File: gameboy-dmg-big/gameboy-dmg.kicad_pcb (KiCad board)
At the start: 2 copper layers, 82.5 x 139.7 mm, 95 parts, among them J1 Conn_01x02, J2 USB_A, J3 Conn_01x08, J4 Conn_01x04, J5 Raspberry_Pi_2_3, J7 USB_B_Micro, J8 Conn_01x02, P1 RK10J_POT, Q1 S8050, SW1 SW_DPDT_x2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

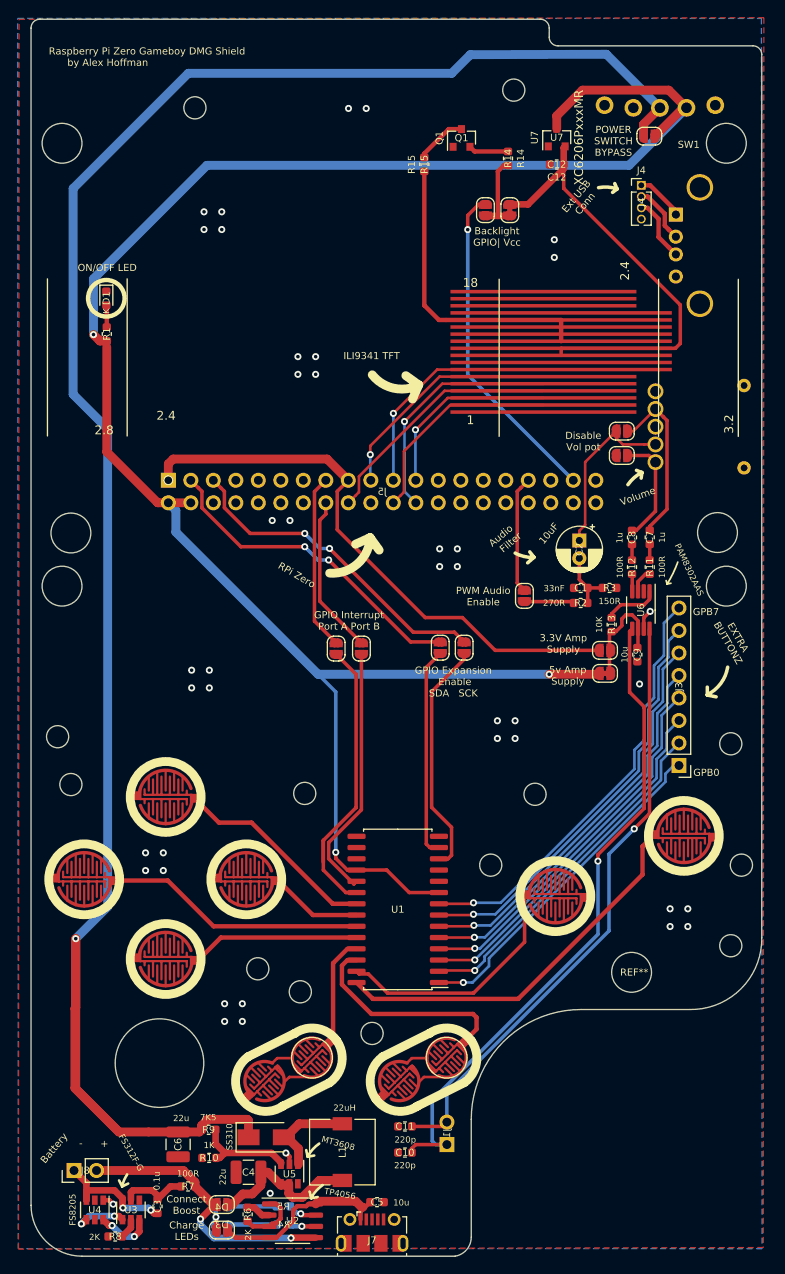
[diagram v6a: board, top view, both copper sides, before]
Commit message: Updated PCBs from initial debugging
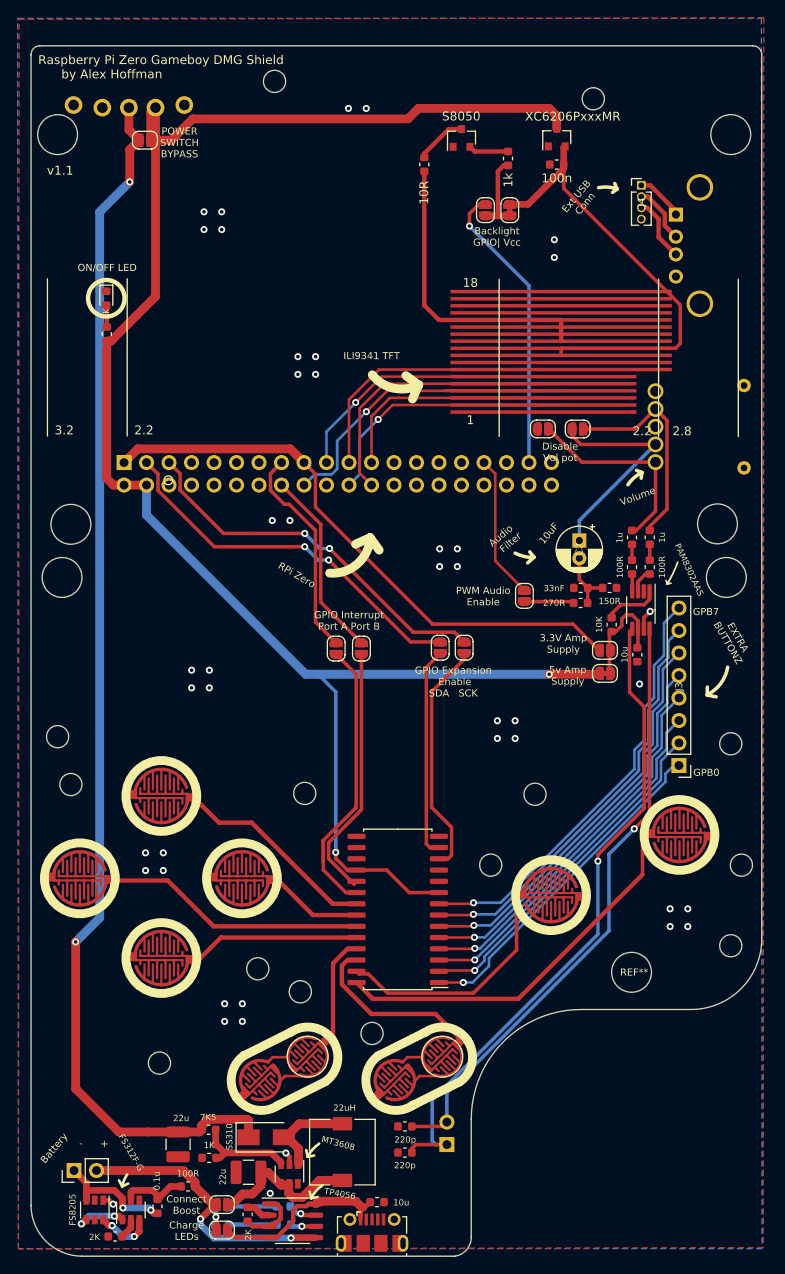
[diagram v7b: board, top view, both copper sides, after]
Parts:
- removed the REF** at (82.5, 77.1)
- removed the REF** at (133.5, 21.1)
- removed the REF** at (97.5, 23.1)
- removed the REF** at (157.5, 27.1)
- removed the REF** at (82.5, 27.1)
- removed the REF** at (83.5, 71.1)
- added REF**: MountingHole_2.5mm, MountingHole:MountingHole_2.5mm, F.Cu at (106.5, 20.1)
- added REF**: MountingHole_4.5mm, MountingHole:MountingHole_4.5mm, F.Cu at (82.5, 76.1)
- added REF**: MountingHole_2.5mm, MountingHole:MountingHole_2.5mm, F.Cu at (142.5, 22.1)
- added REF**: MountingHole_4.5mm, MountingHole:MountingHole_4.5mm, F.Cu at (158.0, 26.1)
- added REF**: MountingHole_4.5mm, MountingHole:MountingHole_4.5mm, F.Cu at (82.0, 26.1)
- added REF**: MountingHole_4.5mm, MountingHole:MountingHole_4.5mm, F.Cu at (83.5, 70.1)
- moved SW1 60.0 mm to (93.0, 23.1)
- moved JP8 56.9 mm to (91.9, 26.8)
- moved JP14 9.40 mm to (136.8, 59.4)
- moved J5 5.39 mm to (89.5, 63.1)
- moved JP10 4.99 mm to (140.7, 59.4)
- moved REF** 0.98 mm to (156.5, 70.1)
- moved REF** 0.98 mm to (157.5, 76.1)
- moved START1 0.50 mm to (120.2, 132.9)
- moved DOWN1 0.50 mm to (93.7, 119.1)
- moved UP1 0.50 mm to (93.7, 100.8)
- moved SELECT1 0.50 mm to (105.0, 132.9)
- moved LEFT1 0.50 mm to (84.5, 110.1)
- moved RIGHT1 0.50 mm to (102.8, 110.1)
- moved A1 0.50 mm to (152.2, 105.2)
- moved B1 0.50 mm to (137.7, 112.0)
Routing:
- net /TP4056_LIPO_BOOST/5V_BOOST: track 232.0 -> 138.6 mm, vias 1 -> 2
- net +5V: track 223.4 -> 199.1 mm, vias 3 -> 2
- net /TFT_DC: track 28.3 -> 46.5 mm, vias 0 -> 1
- net Net-(C8-Pad2): track 12.5 -> 22.7 mm
- net /TFT_CS: track 27.2 -> 33.2 mm, vias 1 -> 0
- net /TFT_RESET: track 24.2 -> 30.1 mm, vias 0 -> 1
- net /TFT_MOSI: track 26.7 -> 32.6 mm
- net /TFT_SCK: track 21.7 -> 27.5 mm, vias 1 -> 0
- net /GPIO_SDA_PI: track 36.8 -> 42.6 mm
- net /GPIO_SCK_PI: track 37.0 -> 42.8 mm
- net Net-(C2-Pad1): track 19.6 -> 25.0 mm
- net Net-(C7-Pad1): track 19.2 -> 24.1 mm
- net /GPIO_INTA_PI: track 19.9 -> 24.3 mm
- net /TFT_BACKLIGHT_GPIO: track 37.4 -> 33.1 mm
- net /START: track 23.9 -> 19.9 mm
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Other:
- board size 82.5 x 139.7 mm -> 82.5 x 136.7 mm
- board text added: "v1.1"
